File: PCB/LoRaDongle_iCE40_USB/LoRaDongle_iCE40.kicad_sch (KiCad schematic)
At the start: 18 parts, among them J1 USB_A, J2 Conn_01x08, J4 Jumper

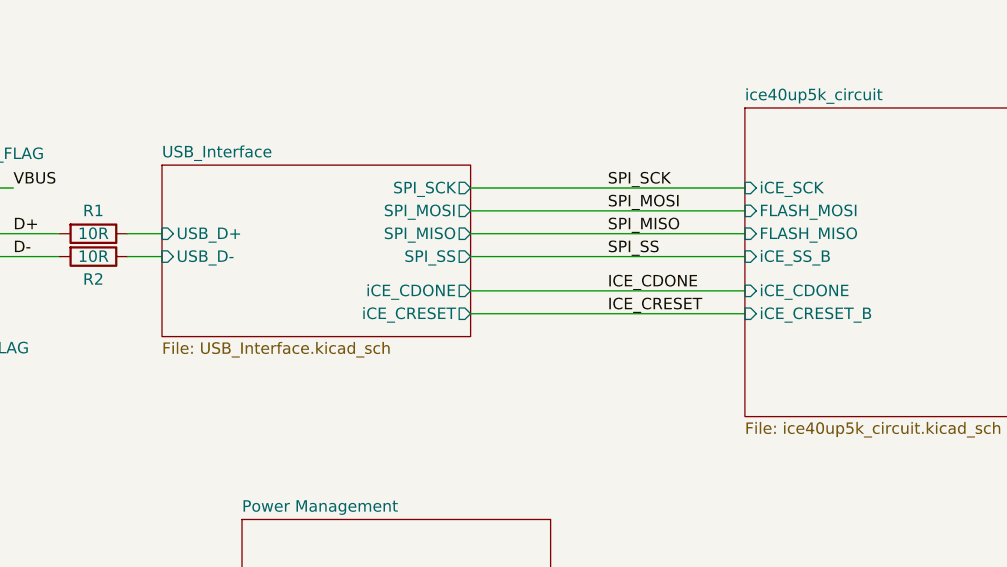
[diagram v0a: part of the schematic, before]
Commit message: updated ftdi and flash chip, removed xilinx project
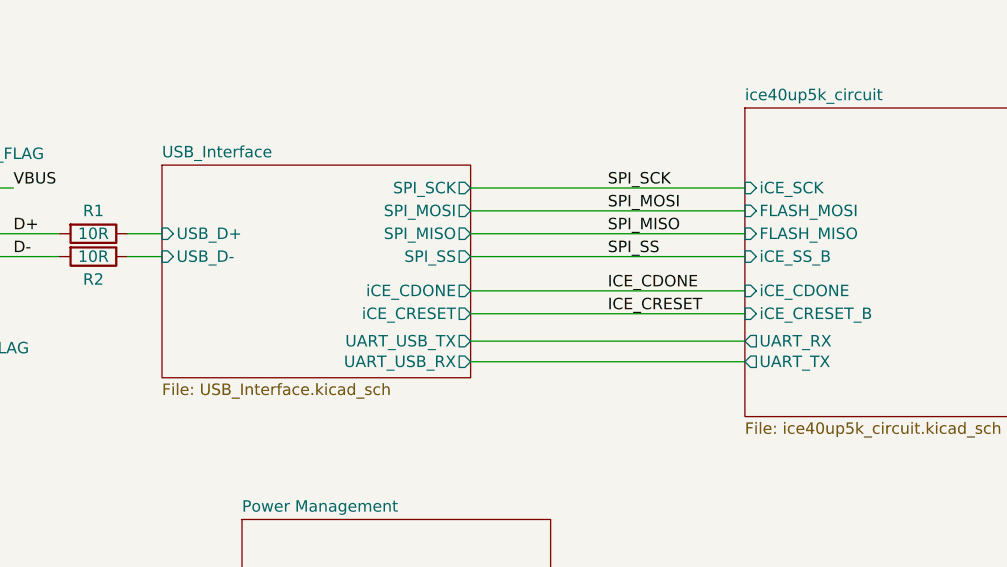
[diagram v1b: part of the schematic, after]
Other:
- sheet USB_Interface ports: added UART_USB_RX, UART_USB_TX; removed none
- sheet ice40up5k_circuit ports: added UART_RX, UART_TX; removed none
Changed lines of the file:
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@@
+    (stroke (width 0) (type default) (color 0 0 0 0))
+  )
+  (wire (pts (xy 92.71 112.014) (xy 123.19 112.014))
     (stroke (width 0) (type default) (color 0 0 0 0))
   )
@@
   )
   (wire (pts (xy 93.98 45.72) (xy 88.9 45.72))
+    (stroke (width 0) (type default) (color 0 0 0 0))
+  )
+  (wire (pts (xy 92.71 109.728) (xy 123.19 109.728))
     (stroke (width 0) (type default) (color 0 0 0 0))
   )
@@
     )
   )
-  (sheet (at 58.42 90.17) (size 34.29 19.05) (fields_autoplaced)
+  (sheet (at 58.42 90.17) (size 34.29 23.622) (fields_autoplaced)
     (stroke (width 0) (type solid) (color 0 0 0 0))
     (fill (color 0 0 0 0.0000))
@@
       (effects (font (size 1.27 1.27)) (justify left bottom))
     )
-    (property "Sheet file" "USB_Interface.kicad_sch" (id 1) (at 58.42 109.8046 0)
+    (property "Sheet file" "USB_Interface.kicad_sch" (id 1) (at 58.42 114.3766 0)
       (effects (font (size 1.27 1.27)) (justify left top))
     )
@@
     (pin "USB_D+" input (at 58.42 97.79 180)
       (effects (font (size 1.27 1.27)) (justify left))
+    )
+    (pin "UART_USB_TX" output (at 92.71 109.728 0)
+      (effects (font (size 1.27 1.27)) (justify right))
+    )
+    (pin "UART_USB_RX" output (at 92.71 112.014 0)
+      (effects (font (size 1.27 1.27)) (justify right))
     )
   )
@@
     (pin "LoRa_!SS" input (at 171.45 107.95 0)
       (effects (font (size 1.27 1.27)) (justify right))
+    )
+    (pin "UART_TX" output (at 123.19 112.014 180)
+      (effects (font (size 1.27 1.27)) (justify left))
+    )
+    (pin "UART_RX" output (at 123.19 109.728 180)
+      (effects (font (size 1.27 1.27)) (justify left))
     )
   )
@@
       (reference "#PWR08") (unit 1) (value "GND") (footprint "")
     )
-    (path "/00000000-0000-0000-0000-0000618aacd4/00000000-0000-0000-0000-00006191a326"
-      (reference "#PWR09") (unit 1) (value "GND") (footprint "")
-    )
     (path "/00000000-0000-0000-0000-0000618aacd4/00000000-0000-0000-0000-00006191a283"
       (reference "#PWR010") (unit 1) (value "GND") (footprint "")
     )
-    (path "/00000000-0000-0000-0000-0000618aacd4/00000000-0000-0000-0000-00006191a1e2"
-      (reference "#PWR011") (unit 1) (value "GND") (footprint "")
-    )
-    (path "/00000000-0000-0000-0000-0000618aacd4/00000000-0000-0000-0000-00006191a1dc"
-      (reference "#PWR012") (unit 1) (value "GND") (footprint "")
-    )
     (path "/00000000-0000-0000-0000-0000618aacd4/00000000-0000-0000-0000-00006191a1ca"
       (reference "#PWR013") (unit 1) (value "GND") (footprint "")
@@
       (reference "#PWR014") (unit 1) (value "GND") (footprint "")
     )
-    (path "/00000000-0000-0000-0000-0000618aacd4/00000000-0000-0000-0000-00006191a22d"
-      (reference "#PWR015") (unit 1) (value "GND") (footprint "")
-    )
-    (path "/00000000-0000-0000-0000-0000618aacd4/00000000-0000-0000-0000-00006191a1bd"
-      (reference "#PWR016") (unit 1) (value "GND") (footprint "")
-    )
     (path "/00000000-0000-0000-0000-0000618aacd4/00000000-0000-0000-0000-00006191a2d8"
       (reference "#PWR017") (unit 1) (value "GND") (footprint "")
@@
       (reference "#PWR0134") (unit 1) (value "+5V") (footprint "")
     )
+    (path "/00000000-0000-0000-0000-0000618aacd4/10b8e1fd-044b-4bc6-b830-5b461bf21ff0"
+      (reference "#PWR?") (unit 1) (value "GND") (footprint "")
+    )
+    (path "/00000000-0000-0000-0000-0000618aacd4/6414fe1f-4637-437f-992a-f4c4eaa1e07e"
+      (reference "#PWR?") (unit 1) (value "GND") (footprint "")
+    )
+    (path "/00000000-0000-0000-0000-0000618aacd4/9777b795-c173-41f9-a92c-93fb2249d773"
+      (reference "#PWR?") (unit 1) (value "GND") (footprint "")
+    )
+    (path "/00000000-0000-0000-0000-0000618aacd4/cf9d1709-b91b-4ca7-9144-43920f88370b"
+      (reference "#PWR?") (unit 1) (value "GND") (footprint "")
+    )
     (path "/00000000-0000-0000-0000-00006141dfda/00000000-0000-0000-0000-000061c195b0"
       (reference "1V2") (unit 1) (value "1.2V") (footprint "TestPoint:TestPoint_Pad_D1.0mm")
@@
       (reference "C9") (unit 1) (value "0.1uF") (footprint "Capacitor_SMD:C_0402_1005Metric_Pad0.74x0.62mm_HandSolder")
     )
-    (path "/00000000-0000-0000-0000-0000618aacd4/00000000-0000-0000-0000-00006191a318"
-      (reference "C10") (unit 1) (value "10nF") (footprint "Capacitor_SMD:C_0402_1005Metric_Pad0.74x0.62mm_HandSolder")
-    )
     (path "/00000000-0000-0000-0000-0000618aacd4/00000000-0000-0000-0000-00006191a27d"
       (reference "C11") (unit 1) (value "4.7uF") (footprint "Capacitor_SMD:C_0402_1005Metric_Pad0.74x0.62mm_HandSolder")
@@
       (reference "C12") (unit 1) (value "0.1uF") (footprint "Capacitor_SMD:C_0402_1005Metric_Pad0.74x0.62mm_HandSolder")
     )
-    (path "/00000000-0000-0000-0000-0000618aacd4/00000000-0000-0000-0000-00006191a2a6"
-      (reference "C13") (unit 1) (value "0.1uF") (footprint "Capacitor_SMD:C_0402_1005Metric_Pad0.74x0.62mm_HandSolder")
-    )
     (path "/00000000-0000-0000-0000-0000618aacd4/00000000-0000-0000-0000-00006191a23a"
       (reference "C14") (unit 1) (value "27pF") (footprint "Capacitor_SMD:C_0603_1608Metric_Pad1.08x0.95mm_HandSolder")
@@
       (reference "C15") (unit 1) (value "27pF") (footprint "Capacitor_SMD:C_0603_1608Metric_Pad1.08x0.95mm_HandSolder")
     )
-    (path "/00000000-0000-0000-0000-0000618aacd4/00000000-0000-0000-0000-00006191a29f"
-      (reference "C16") (unit 1) (value "0.1uF") (footprint "Capacitor_SMD:C_0402_1005Metric_Pad0.74x0.62mm_HandSolder")
-    )
     (path "/00000000-0000-0000-0000-0000618aacd4/00000000-0000-0000-0000-00006191a298"
       (reference "C17") (unit 1) (value "4.7uF") (footprint "Capacitor_SMD:C_0402_1005Metric_Pad0.74x0.62mm_HandSolder")
@@
       (reference "C52") (unit 1) (value "12pF") (footprint "Capacitor_SMD:C_0402_1005Metric_Pad0.74x0.62mm_HandSolder")
     )
+    (path "/00000000-0000-0000-0000-0000618aacd4/23fcaf73-694b-4c79-a85b-ce0a2617c5a4"
+      (reference "C?") (unit 1) (value "0.1uF") (footprint "Capacitor_SMD:C_0402_1005Metric_Pad0.74x0.62mm_HandSolder")
+    )
+    (path "/00000000-0000-0000-0000-0000618aacd4/3163215e-d467-491e-868a-315935e83560"
+      (reference "C?") (unit 1) (value "0.1uF") (footprint "Capacitor_SMD:C_0402_1005Metric_Pad0.74x0.62mm_HandSolder")
+    )
+    (path "/00000000-0000-0000-0000-0000618aacd4/61bfbc67-1815-4018-9994-f0ad20f41204"
+      (reference "C?") (unit 1) (value "3.3uF") (footprint "")
+    )
+    (path "/00000000-0000-0000-0000-0000618aacd4/6b878260-6e1f-4b81-9067-ac12523adce1"
+      (reference "C?") (unit 1) (value "0.1uF") (footprint "Capacitor_SMD:C_0402_1005Metric_Pad0.74x0.62mm_HandSolder")
+    )
     (path "/00000000-0000-0000-0000-000061db206f"
       (reference "CDNE1") (unit 1) (value "iCE_CDONE") (footprint "TestPoint:TestPoint_Pad_D1.0mm")
@@
       (reference "IC2") (unit 1) (value "ICE40UP5K-UWG30ITR1K") (footprint "ICE40UP5K-UWG30ITR1K_KiCad:BGA30C40P5X6_211X254X60")
     )
-    (path "/00000000-0000-0000-0000-0000618d30e5/00000000-0000-0000-0000-0000619d2169"
-      (reference "IC3") (unit 1) (value "N25Q032A13ESC40F") (footprint "N25Q032A13ESC40F:SOIC127P600X175-8N")
-    )
     (path "/00000000-0000-0000-0000-00006134135c"
       (reference "J1") (unit 1) (value "USB_A") (footprint "Connector_USB:USB_A_CNCTech_1001-011-01101_Horizontal")
@@
     )
     (path "/00000000-0000-0000-0000-0000618aacd4/00000000-0000-0000-0000-00006191a312"
-      (reference "R8") (unit 1) (value "10K") (footprint "Resistor_SMD:R_0402_1005Metric_Pad0.72x0.64mm_HandSolder")
+      (reference "R8") (unit 1) (value "1K") (footprint "Resistor_SMD:R_0402_1005Metric_Pad0.72x0.64mm_HandSolder")
     )
     (path "/00000000-0000-0000-0000-0000618aacd4/00000000-0000-0000-0000-00006191a215"
@@
       (reference "R21") (unit 1) (value "100R") (footprint "Resistor_SMD:R_0402_1005Metric_Pad0.72x0.64mm_HandSolder")
     )
+    (path "/00000000-0000-0000-0000-0000618aacd4/658ac0f3-049c-46e5-8dca-a07e1a9af2c7"
+      (reference "R?") (unit 1) (value "10K") (footprint "Resistor_SMD:R_0402_1005Metric_Pad0.72x0.64mm_HandSolder")
+    )
+    (path "/00000000-0000-0000-0000-0000618aacd4/984e32cc-1554-48f3-8a4a-24a036aec6d1"
+      (reference "R?") (unit 1) (value "10K") (footprint "Resistor_SMD:R_0402_1005Metric_Pad0.72x0.64mm_HandSolder")
+    )
     (path "/00000000-0000-0000-0000-000061d57b0f"
       (reference "RESET1") (unit 1) (value "LoRA_~RESET") (footprint "TestPoint:TestPoint_Pad_D1.0mm")
@@
       (reference "U1") (unit 1) (value "RP550K001A-TR") (footprint "RP550K001A-TR_KiCad:SON50P270X300X60-13N")
     )
-    (path "/00000000-0000-0000-0000-0000618aacd4/00000000-0000-0000-0000-00006191a1eb"
-      (reference "U2") (unit 1) (value "FT232H") (footprint "Package_QFP:LQFP-48_7x7mm_P0.5mm")
-    )
     (path "/00000000-0000-0000-0000-0000614f0720/00000000-0000-0000-0000-000061cbfd90"
       (reference "U3") (unit 1) (value "SX1261IMLTRT") (footprint "sx1261-footprint:Semtech-QFN24-0-0-0")
@@
       (reference "U4") (unit 1) (value "SKY13587-378LF") (footprint "SW_SKYA21012:SW_SKYA21012")
     )
+    (path "/00000000-0000-0000-0000-0000618d30e5/b4b3688b-80ae-4639-b202-7fe415fc1c6e"
+      (reference "U?") (unit 1) (value "W25Q128JVS") (footprint "Package_SO:SOIC-8_5.23x5.23mm_P1.27mm")
+    )
+    (path "/00000000-0000-0000-0000-0000618aacd4/ea23d709-947e-4855-b185-6cda7c098dbf"
+      (reference "U?") (unit 1) (value "FT2232HL") (footprint "Package_QFP:LQFP-64_10x10mm_P0.5mm")
+    )
     (path "/00000000-0000-0000-0000-0000618d30e5/00000000-0000-0000-0000-000061bb2826"

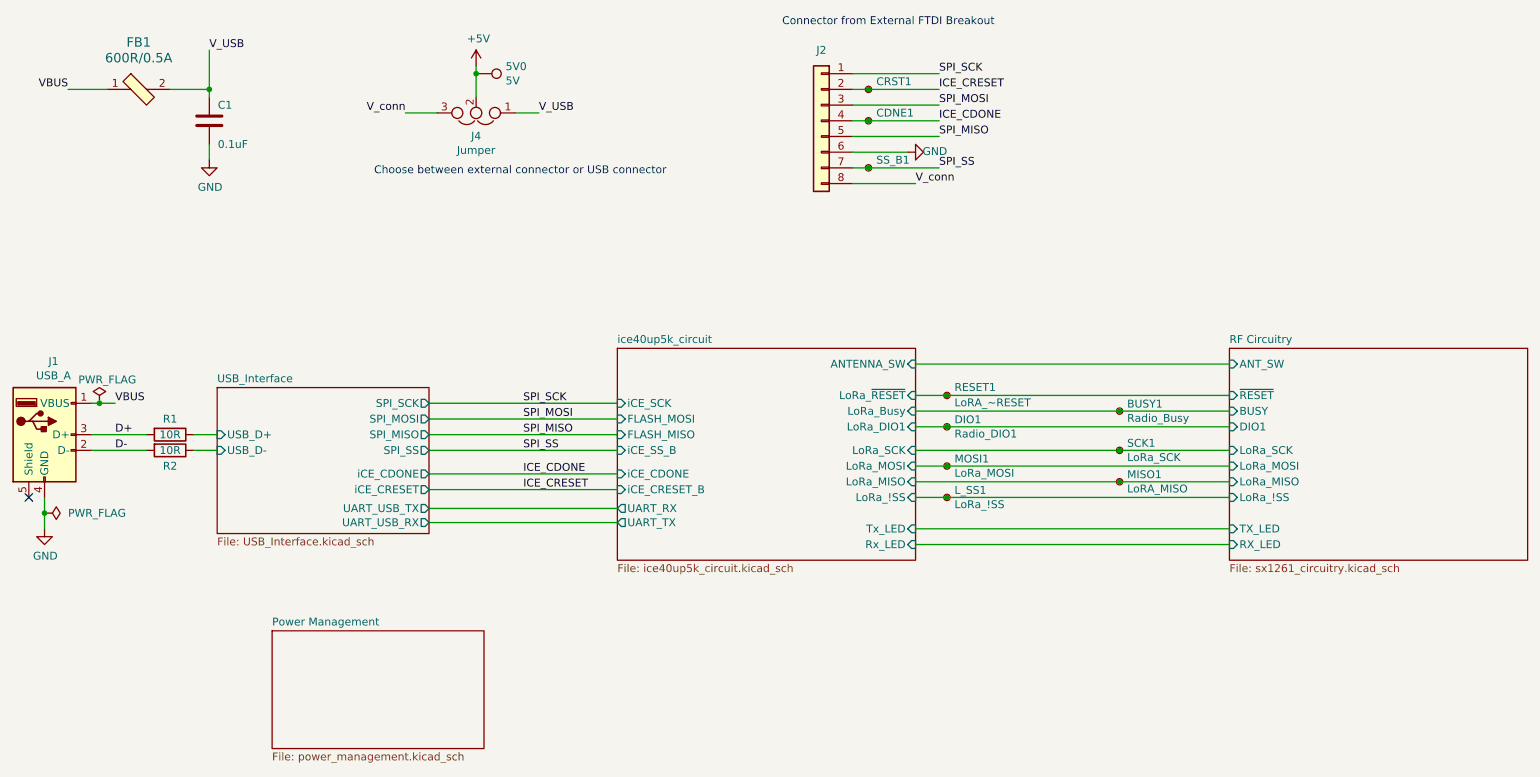
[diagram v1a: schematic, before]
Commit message: updated jumpers, connectors and testpoints
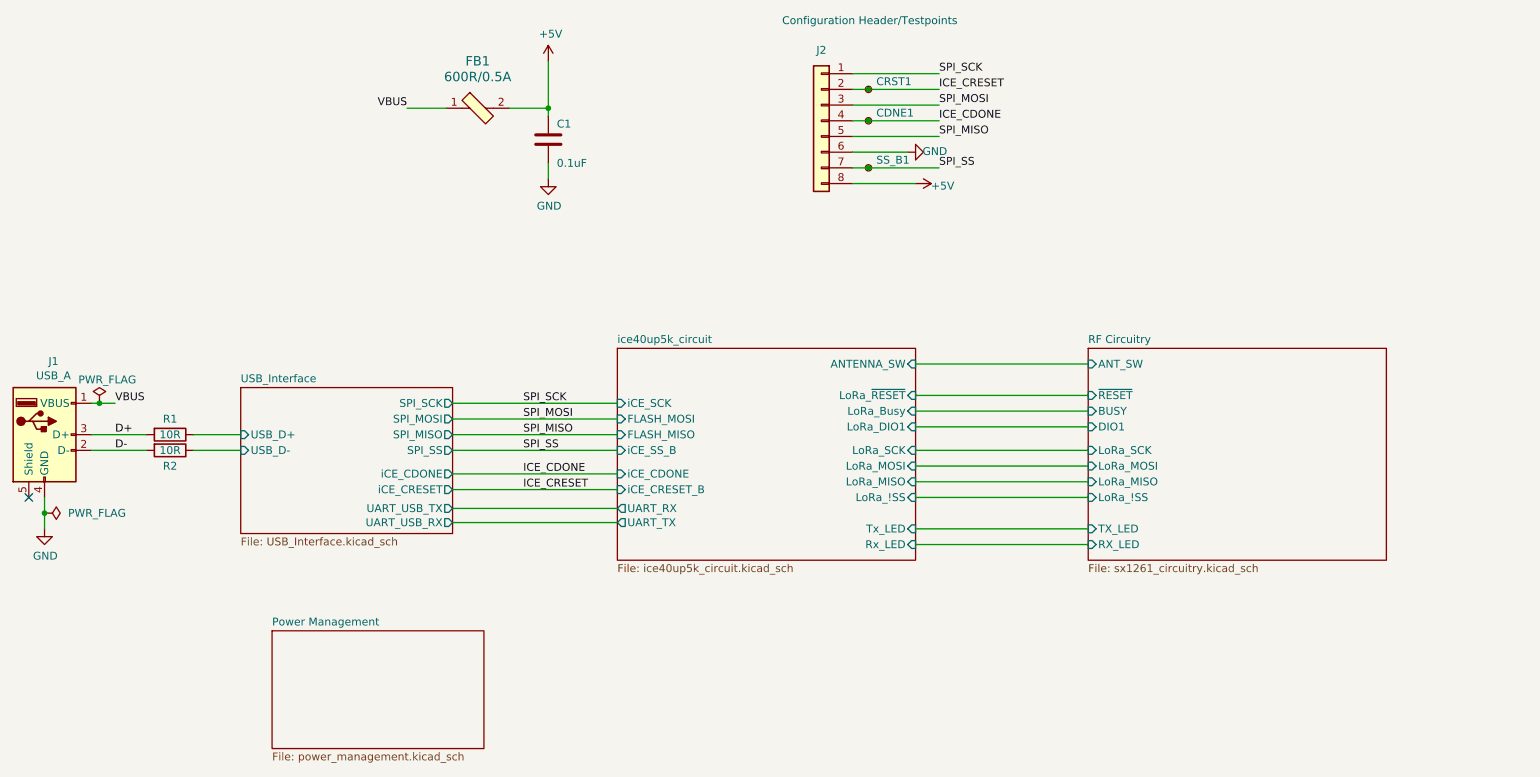
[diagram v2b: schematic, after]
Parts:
- removed 5V0: 5V, TestPoint:TestPoint_Pad_D1.0mm, symbol Connector:TestPoint
- removed BUSY1: Radio_Busy, TestPoint:TestPoint_Pad_D1.0mm, symbol Connector:TestPoint_Small
- removed DIO1: Radio_DIO1, TestPoint:TestPoint_Pad_D1.0mm, symbol Connector:TestPoint_Small
- removed J4: Jumper, Connector_PinHeader_2.54mm:PinHeader_1x03_P2.54mm_Vertical, symbol Device:Jumper_NC_Dual
- removed L_SS1: LoRa_!SS, TestPoint:TestPoint_Pad_D1.0mm, symbol Connector:TestPoint_Small
- removed MISO1: LoRA_MISO, TestPoint:TestPoint_Pad_D1.0mm, symbol Connector:TestPoint_Small
- removed MOSI1: LoRa_MOSI, TestPoint:TestPoint_Pad_D1.0mm, symbol Connector:TestPoint_Small
- removed RESET1: LoRA_~RESET, TestPoint:TestPoint_Pad_D1.0mm, symbol Connector:TestPoint_Small
- removed SCK1: LoRa_SCK, TestPoint:TestPoint_Pad_D1.0mm, symbol Connector:TestPoint_Small
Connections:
- net V_USB is gone; now on net +5V: C1.2, FB1.2
- net V_conn is gone; now on net +5V: J2.8 (Pin_8)
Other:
- note added: "Configuration Header/Testpoints"
- note removed: "Choose between external connector or USB connector"
- note removed: "Connector from External FTDI Breakout"
- moved on the sheet: C1, FB1

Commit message: updated layout and routing
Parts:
- removed CDNE1: iCE_CDONE, TestPoint:TestPoint_Pad_D1.0mm, symbol Connector:TestPoint_Small
- removed CRST1: iCE_CRESET, TestPoint:TestPoint_Pad_D1.0mm, symbol Connector:TestPoint_Small
- removed SS_B1: iCE_SS_B, TestPoint:TestPoint_Pad_D1.0mm, symbol Connector:TestPoint_Small
